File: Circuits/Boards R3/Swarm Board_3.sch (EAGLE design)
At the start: 139 parts, among them CON1 ISP(2X3), CON2 MAIN_CONNECTOR_14SMD, CON4 HEADER_3X1, CON5 HEADER_3X1, CON7 MAIN_CONNECTOR_8, M1 VIBMOTOR, T1 TEFT4300, T10 TEFT4300, T11 NPN2N2222, T12 SI2333DS-T1, T13 NPN2N2222, T14 NPN2N2222, T15 NPN2N2222, T16 NPN2N2222, T17 NPN2N2222, T18 NPN2N2222, T19 IRLML6244TR, T2 TEFT4300, T20 IRLML6244TR, T21 IRLML6244TR, T22 IRLML6244TR, T23 IRLML6244TR, T3 NPN2N2222, T4 TEFT4300, T5 TEFT4300, T6 TEFT4300, T7 TEFT4300, T8 TEFT4300, T9 TEFT4300, U1 ATMEGA324P, U2 MCP73833, U3 ATMEGA1281, U4 MCP9700A, U5 AH182, U6 AH182, U7 QRE1113, U8 QRE1113, U9 QRE1113

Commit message: MORE STUFF
LEDS, TX/RX, WHATEVER
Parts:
- LED11, LED12: value (none) -> RED
- LED14, LED15: value (none) -> GREEN
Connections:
- new net LED5: R56.1
- net LED4: no longer R53.1, R55.1, R56.1
- net MISO: now also R55.1
- net MOSI: now also R53.1
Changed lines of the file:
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@@
 <part name="U9" library="Passive" deviceset="QRE1113" device=""/>
 <part name="R52" library="Passive" deviceset="RES" device="0603" value="100"/>
-<part name="LED11" library="Passive" deviceset="LED" device="0603"/>
+<part name="LED11" library="Passive" deviceset="LED" device="0603" value="RED"/>
 <part name="R53" library="Passive" deviceset="RES" device="0603" value="1k"/>
 <part name="P+3" library="Supply" deviceset="+3V" device=""/>
-<part name="LED12" library="Passive" deviceset="LED" device="0603"/>
+<part name="LED12" library="Passive" deviceset="LED" device="0603" value="RED"/>
 <part name="R54" library="Passive" deviceset="RES" device="0603" value="1k"/>
 <part name="P+8" library="Supply" deviceset="+3V" device=""/>
-<part name="LED14" library="Passive" deviceset="LED" device="0603"/>
+<part name="LED14" library="Passive" deviceset="LED" device="0603" value="GREEN"/>
 <part name="R55" library="Passive" deviceset="RES" device="0603" value="1k"/>
 <part name="P+11" library="Supply" deviceset="+3V" device=""/>
-<part name="LED15" library="Passive" deviceset="LED" device="0603"/>
+<part name="LED15" library="Passive" deviceset="LED" device="0603" value="GREEN"/>
 <part name="R56" library="Passive" deviceset="RES" device="0603" value="1k"/>
 <part name="P+17" library="Supply" deviceset="+3V" device=""/>
@@
 <label x="-53.34" y="38.1" size="1.778" layer="95"/>
 </segment>
+<segment>
+<pinref part="R55" gate="G$1" pin="1"/>
+<wire x1="-86.36" y1="-48.26" x2="-86.36" y2="-50.8" width="0.1524" layer="91"/>
+<label x="-86.36" y="-50.8" size="1.778" layer="91" rot="R270" xref="yes"/>
+</segment>
 </net>
 <net name="TEMPSENSE" class="0">
@@
 <wire x1="-76.2" y1="40.64" x2="-30.48" y2="40.64" width="0.1524" layer="91"/>
 <label x="-53.34" y="40.64" size="1.778" layer="95"/>
+</segment>
+<segment>
+<pinref part="R53" gate="G$1" pin="1"/>
+<wire x1="-106.68" y1="-48.26" x2="-106.68" y2="-50.8" width="0.1524" layer="91"/>
+<label x="-106.68" y="-50.8" size="1.778" layer="91" rot="R270" xref="yes"/>
 </segment>
 </net>
@@
 <net name="LED4" class="0">
 <segment>
-<pinref part="R53" gate="G$1" pin="1"/>
-<wire x1="-106.68" y1="-48.26" x2="-106.68" y2="-50.8" width="0.1524" layer="91"/>
-<label x="-106.68" y="-50.8" size="1.778" layer="91" rot="R270" xref="yes"/>
-</segment>
-<segment>
 <pinref part="R54" gate="G$1" pin="1"/>
 <wire x1="-96.52" y1="-48.26" x2="-96.52" y2="-50.8" width="0.1524" layer="91"/>
 <label x="-96.52" y="-50.8" size="1.778" layer="91" rot="R270" xref="yes"/>
-</segment>
-<segment>
-<pinref part="R55" gate="G$1" pin="1"/>
-<wire x1="-86.36" y1="-48.26" x2="-86.36" y2="-50.8" width="0.1524" layer="91"/>
-<label x="-86.36" y="-50.8" size="1.778" layer="91" rot="R270" xref="yes"/>
-</segment>
-<segment>
-<pinref part="R56" gate="G$1" pin="1"/>
-<wire x1="-76.2" y1="-48.26" x2="-76.2" y2="-50.8" width="0.1524" layer="91"/>
-<label x="-76.2" y="-50.8" size="1.778" layer="91" rot="R270" xref="yes"/>
 </segment>
 </net>
@@
 </segment>
 </net>
+<net name="LED5" class="0">
+<segment>
+<pinref part="R56" gate="G$1" pin="1"/>
+<wire x1="-76.2" y1="-48.26" x2="-76.2" y2="-50.8" width="0.1524" layer="91"/>
+<label x="-76.2" y="-50.8" size="1.778" layer="91" rot="R270" xref="yes"/>
+</segment>
+</net>

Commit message: picked new 3v regulator
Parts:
- added TST1, TST2: TESTPOINT, Mechanical:TESTPOINT
- V1: value MCP1700-3002E -> XC6210B302; device PowerIC:MCP1700-3002E -> PowerIC:XC6210B302
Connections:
- removed net SCL: ANT4.P$1, U3.PD0(SCL/INT0)
- removed net SDA: ANT2.P$1, U3.PD1(SDA/INT1)
- new net CRX: ANT4.P$1, U3.PE0(RXD0/PCINT8/PDI)
- new net CTX: ANT2.P$1, U3.PE1(TXD0/PDO)
- new net DEBUG1: TST1.P$1
- new net DEBUG2: TST2.P$1
- new net VIBE: R58.1
- net +3V: now also C16.1, C9.1, M1.+VM, U$1.VM, V1.VOUT; no longer V1.OUT
- net +VRAW: now also V1.EN, V1.VIN; no longer C16.1, C9.1, M1.+VM, U$1.VM, V1.IN
- net DATAANTENNA: now also U3.PD3(TXD1/INT3); no longer U1.PD1(PCINT25/TXD0)
- net DISTANCELED: no longer R58.1
- net N$8: now also U3.PD2(RXD1/INT2); no longer U1.PD0(PCINT24/RXD0)
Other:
- moved on the sheet: CON5

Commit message: ready to route
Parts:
- removed U9: QRE1113, Passive:QRE1113
- added C17: 10uf, Passive:CAPPTH
- added R25, R59, R6, R60, R61, R62: 10k, Passive:RES0603
- C2: value 10uf -> 1uf; device Passive:CAP0805 -> Passive:CAP0603
- C3, C8: value 1uf -> .1uf
- R34: value 22k -> 10k
- R52: value 100 -> 10k
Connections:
- net IRBUMBER renamed ????
- removed net SIRBUMPER: CON7.5, R34.2, U9.E
- new net LED6: R55.1
- new net LED7: R56.1
- new net N$49: R25.2
- new net N$50: R34.2
- new net N$51: R52.2
- new net N$52: R59.2
- new net N$53: R60.2
- new net N$54: R61.2
- new net N$55: R62.2
- new net N$56: U3.PD0(SCL/INT0)
- new net N$57: U3.PD1(SDA/INT1)
- new net N$58: U3.PE6(T3/INT6)
- new net N$59: U3.PE7(ICP3/CLKO/INT7)
- new net PB0: U3.PB0(!SS!/PCINT0)
- new net PB4: U3.PB4(OC2A/PCINT4)
- new net PB5: U3.PB5(OC1A/PCINT5)
- new net PB6: U3.PB6(OC1B/PCINT6)
- new net PB7: U3.PB7(OC0A/OC1C/PCINT7)
- new net S????: CON7.5
- net +3V: now also C17.1
- net APWM: now also U3.PE3(OC3A/AIN1)
- net BPWM: now also U3.PE4(OC3B/INT4)
- net BUZZER: now also U3.PG5(OC0B)
- net GND: now also C17.2
- net LED4: now also R53.1, U3.PE5(OC3C/INT5); no longer R54.1
- net LED5: now also R54.1; no longer R56.1
- net MISO: no longer R55.1
- net MOSI: no longer R53.1
- net N$2: no longer R52.2
- net N$42: now also R6.2; no longer R52.1, U9.CT
- net RX1: now also R6.1
- net RX2: now also R25.1
- net RX3: now also R34.1
- net RX4: now also R52.1
- net RX5: now also R59.1
- net RX6: now also R60.1
- net RX7: now also R61.1
- net RX8: now also R62.1
- net S+VSENSE: no longer U9.AN, U9.C
- net SGND: no longer R34.1
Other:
- moved on the sheet: C2, R34, R52, U3

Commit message: more routing
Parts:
- removed U1: ATMEGA324P, DigitalIC:ATMEGA324P
- C17: device Passive:CAPPTH -> Passive:CAP0805
- C9: value 1uf -> 10uf; device Passive:CAP0603 -> Passive:CAP0805
- CON2: value MAIN_CONNECTOR_14SMD -> MAIN_CONNECTOR_14; device Mechanical:MAIN_CONNECTOR_14SMD -> Mechanical:MAIN_CONNECTOR_14
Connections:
- removed net IRBUMPER: U1.PA3(ADC3/PCINT3)
- new net N$60: U3.PC0(A8)
- new net N$61: U3.PC1(A9)
- new net N$62: U3.PC2(A10)
- new net N$63: U3.PC3(A11)
- new net N$64: U3.PC4(A12)
- new net N$65: U3.PC5(A13)
- new net N$66: U3.PC6(A14)
- new net N$67: U3.PC7(A15)
- new net N$68: U3.PD4(ICP1)
- new net N$69: U3.PD5(XCK1)
- new net N$70: U3.PD6(T1)
- new net N$71: U3.PD7(T0)
- new net N$72: U3.PF0(ADC0)
- new net N$73: U3.PF1(ADC1)
- new net N$74: U3.PF2(ADC2)
- new net N$75: U3.PF3(ADC3)
- new net N$76: U3.PF4(ADC4/TCK)
- new net N$77: U3.PF5(ADC5/TMS)
- new net N$78: U3.PF6(ADC6/TDO)
- new net N$79: U3.PF7(ADC7/TDI)
- new net N$80: U3.PG0(!WR!)
- new net N$81: U3.PG1(!RD!)
- new net N$82: U3.PG2(ALE)
- new net N$83: U3.PG3(TOSC2)
- new net N$84: U3.PG4(TOSC1)
- new net N$85: U3.PA0(AD0)
- new net N$86: U3.PA1(AD1)
- new net N$87: U3.PA2(AD2)
- new net N$88: U3.PA3(AD3)
- new net N$89: U3.PA4(AD4)
- new net N$90: U3.PA5(AD5)
- new net N$91: U3.PA6(AD6)
- new net N$92: U3.PA7(AD7)
- net AIN1: no longer U1.PD5(PCINT29/OC1A)
- net AIN2: no longer U1.PC0(PCINT16/SCL)
- net APWM: no longer U1.PD7(PCINT31/OC2A)
- net BIN1: no longer U1.PD3(PCINT27/TXD1/INT1)
- net BIN2: no longer U1.PD2(PCINT26/RXD1/INT0)
- net BPWM: no longer U1.PD6(PCINT30/OC2B/ICP)
- net BUZZER: no longer U1.PB4(!SS!/OC0B/PCINT12)
- net CHGDETECT: no longer U1.PB0(XCK0/T0/PCINT8)
- net CHGSTATUS: no longer U1.PB1(T1/CLKO/PCINT9)
- net DISTANCELED: no longer U1.PA6(ADC6/PCINT6)
- net DISTANCERECEIVE: no longer U1.PA7(ADC7/PCINT7)
- net IRENABLE: no longer U1.PA4(ADC4/PCINT4)
- net LED1: no longer U1.PB2(AIN0/INT2/PCINT10)
- net LED2: no longer U1.PB3(AIN1/OC0A/PCINT11)
- net LIGHTSENSE: no longer U1.PA5(ADC5/PCINT5)
- net LINESENSE1: no longer U1.PA1(ADC1/PCINT1)
- net LINESENSE2: no longer U1.PA2(ADC2/PCINT2)
- net RX1: no longer U1.PC2(PCINT18/TCK)
- net RX2: no longer U1.PC3(PCINT19/TMS)
- net RX3: no longer U1.PC4(TDO/PCINT20)
- net RX4: no longer U1.PC5(TDI/PCINT21)
- net RX5: no longer U1.PC6(TOSC1/PCINT22)
- net RX6: no longer U1.PC7(TOSC2/PCINT23)
- net STBY: no longer U1.PD4(PCINT28/XCK1/OC1B)
- net TRANSMITLEDS: no longer U1.PC1(PCINT17/SDA)
- net VBATSENSE: no longer U1.PA0(ADC0/PCINT0)
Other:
- moved on the sheet: C8, C9

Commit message: more routing
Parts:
- added W1, W2, W3: WHISKER, Mechanical:WHISKER
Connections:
- removed net ????: CON2.12
- removed net N$40: R48.1
- removed net N$41: R49.1
- removed net N$42: R6.2
- removed net N$49: R25.2
- removed net N$50: R34.2
- removed net N$51: R52.2
- removed net N$52: R59.2
- removed net N$53: R60.2
- removed net N$54: R61.2
- removed net N$55: R62.2
- removed net N$56: U3.PD0(SCL/INT0)
- removed net N$57: U3.PD1(SDA/INT1)
- removed net N$60: U3.PC0(A8)
- removed net N$61: U3.PC1(A9)
- removed net N$62: U3.PC2(A10)
- removed net N$63: U3.PC3(A11)
- removed net N$64: U3.PC4(A12)
- removed net N$65: U3.PC5(A13)
- removed net N$66: U3.PC6(A14)
- removed net N$67: U3.PC7(A15)
- removed net N$68: U3.PD4(ICP1)
- removed net N$72: U3.PF0(ADC0)
- removed net N$73: U3.PF1(ADC1)
- removed net N$74: U3.PF2(ADC2)
- removed net N$75: U3.PF3(ADC3)
- removed net N$76: U3.PF4(ADC4/TCK)
- removed net N$77: U3.PF5(ADC5/TMS)
- removed net N$78: U3.PF6(ADC6/TDO)
- removed net N$79: U3.PF7(ADC7/TDI)
- removed net N$81: U3.PG1(!RD!)
- removed net N$85: U3.PA0(AD0)
- removed net N$86: U3.PA1(AD1)
- removed net N$87: U3.PA2(AD2)
- removed net N$88: U3.PA3(AD3)
- removed net N$89: U3.PA4(AD4)
- removed net N$90: U3.PA5(AD5)
- removed net N$91: U3.PA6(AD6)
- removed net N$92: U3.PA7(AD7)
- removed net S????: CON7.5
- removed net SLINSENSE2: R33.2, U7.E
- net AIN1: now also U3.PA4(AD4)
- net AIN2: now also U3.PA3(AD3)
- net BIN1: now also U3.PA6(AD6)
- net BIN2: now also U3.PA7(AD7)
- net CHGDETECT: now also U3.PF2(ADC2)
- net CHGSTATUS: now also U3.PF1(ADC1)
- net DISTANCELED: now also U3.PA1(AD1)
- net DISTANCERECEIVE: now also U3.PF5(ADC5/TMS)
- net ENCA: now also U3.PD0(SCL/INT0)
- net ENCB: now also U3.PD1(SDA/INT1)
- net IRENABLE: now also U3.PC7(A15)
- net LED1: now also U3.PC4(A12)
- net LED2: now also U3.PC3(A11)
- net LED3: now also U3.PC2(A10)
- net LED5: now also U3.PG1(!RD!)
- net LED6: now also U3.PC0(A8)
- net LED7: now also U3.PA2(AD2)
- net LEFTBUMPER: now also U3.PC5(A13)
- net LIGHTSENSE: now also U3.PF6(ADC6/TDO)
- net LINESENSE1: now also U3.PF3(ADC3)
- net LINESENSE2: now also U3.PF4(ADC4/TCK)
- net MISO: now also R61.2
- net MOSI: now also R6.2
- net PB0: now also R34.2
- net PB4: now also R60.2
- net PB5: now also R59.2
- net PB6: now also R52.2
- net PB7: now also R62.2
- net RIGHTBUMPER: now also U3.PC6(A14)
- net S+VSENSE: now also W3.P$1; no longer R48.2, R49.2
- net SCK: now also R25.2
- net SEN: now also U3.PE2(XCK0/AIN0)
- net SGND: now also R48.1, R49.1
- net SLEFTBUMPER: now also R49.2, W1.P$1
- net SLINESENSE2: now also R33.2, U7.E
- net SRIGHTBUMPER: now also R48.2, W2.P$1
- net STBY: now also U3.PA5(AD5)
- net TEMPSENSE: now also U3.PF7(ADC7/TDI)
- net TRANSMITLEDS: now also U3.PD4(ICP1)
- net VBATSENSE: now also U3.PF0(ADC0)
- net VIBE: now also U3.PC1(A9)
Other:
- moved on the sheet: R48, R49

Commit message: schematic at 100%
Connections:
- removed net N$58: U3.PE6(T3/INT6)
- removed net N$59: U3.PE7(ICP3/CLKO/INT7)
- removed net N$69: U3.PD5(XCK1)
- removed net N$70: U3.PD6(T1)
- removed net N$71: U3.PD7(T0)
- removed net N$80: U3.PG0(!WR!)
- removed net N$82: U3.PG2(ALE)
- removed net N$83: U3.PG3(TOSC2)
- removed net N$84: U3.PG4(TOSC1)
- net DEBUG1: now also U3.PG2(ALE)
- net DEBUG2: now also U3.PG0(!WR!)
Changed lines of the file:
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@@
 <pinref part="TST1" gate="G$1" pin="P$1"/>
+</segment>
+<segment>
+<pinref part="U3" gate="G$1" pin="PG2(ALE)"/>
+<wire x1="38.1" y1="-33.02" x2="40.64" y2="-33.02" width="0.1524" layer="91"/>
+<label x="40.64" y="-33.02" size="1.778" layer="91" xref="yes"/>
 </segment>
 </net>
@@
 <label x="-50.8" y="-50.8" size="1.778" layer="91" rot="R270" xref="yes"/>
 <pinref part="TST2" gate="G$1" pin="P$1"/>
+</segment>
+<segment>
+<pinref part="U3" gate="G$1" pin="PG0(!WR!)"/>
+<wire x1="38.1" y1="-27.94" x2="40.64" y2="-27.94" width="0.1524" layer="91"/>
+<label x="40.64" y="-27.94" size="1.778" layer="91" xref="yes"/>
 </segment>
 </net>
@@
 </segment>
 </net>
-<net name="N$58" class="0">
-<segment>
-<pinref part="U3" gate="G$1" pin="PE6(T3/INT6)"/>
-<wire x1="38.1" y1="2.54" x2="40.64" y2="2.54" width="0.1524" layer="91"/>
-<label x="40.64" y="2.54" size="1.778" layer="91" xref="yes"/>
-</segment>
-</net>
-<net name="N$59" class="0">
-<segment>
-<pinref part="U3" gate="G$1" pin="PE7(ICP3/CLKO/INT7)"/>
-<wire x1="38.1" y1="0" x2="40.64" y2="0" width="0.1524" layer="91"/>
-<label x="40.64" y="0" size="1.778" layer="91" xref="yes"/>
-</segment>
-</net>
-<net name="N$69" class="0">
-<segment>
-<pinref part="U3" gate="G$1" pin="PD5(XCK1)"/>
-<wire x1="38.1" y1="27.94" x2="40.64" y2="27.94" width="0.1524" layer="91"/>
-</segment>
-</net>
-<net name="N$70" class="0">
-<segment>
-<pinref part="U3" gate="G$1" pin="PD6(T1)"/>
-<wire x1="38.1" y1="25.4" x2="40.64" y2="25.4" width="0.1524" layer="91"/>
-</segment>
-</net>
-<net name="N$71" class="0">
-<segment>
-<pinref part="U3" gate="G$1" pin="PD7(T0)"/>
-<wire x1="38.1" y1="22.86" x2="40.64" y2="22.86" width="0.1524" layer="91"/>
-</segment>
-</net>
-<net name="N$80" class="0">
-<segment>
-<pinref part="U3" gate="G$1" pin="PG0(!WR!)"/>
-<wire x1="38.1" y1="-27.94" x2="40.64" y2="-27.94" width="0.1524" layer="91"/>
-</segment>
-</net>
-<net name="N$82" class="0">
-<segment>
-<pinref part="U3" gate="G$1" pin="PG2(ALE)"/>
-<wire x1="38.1" y1="-33.02" x2="40.64" y2="-33.02" width="0.1524" layer="91"/>
-</segment>
-</net>
-<net name="N$83" class="0">
-<segment>
-<pinref part="U3" gate="G$1" pin="PG3(TOSC2)"/>
-<wire x1="38.1" y1="-35.56" x2="40.64" y2="-35.56" width="0.1524" layer="91"/>
-</segment>
-</net>
-<net name="N$84" class="0">
-<segment>
-<pinref part="U3" gate="G$1" pin="PG4(TOSC1)"/>
-<wire x1="38.1" y1="-38.1" x2="40.64" y2="-38.1" width="0.1524" layer="91"/>
-</segment>
-</net>

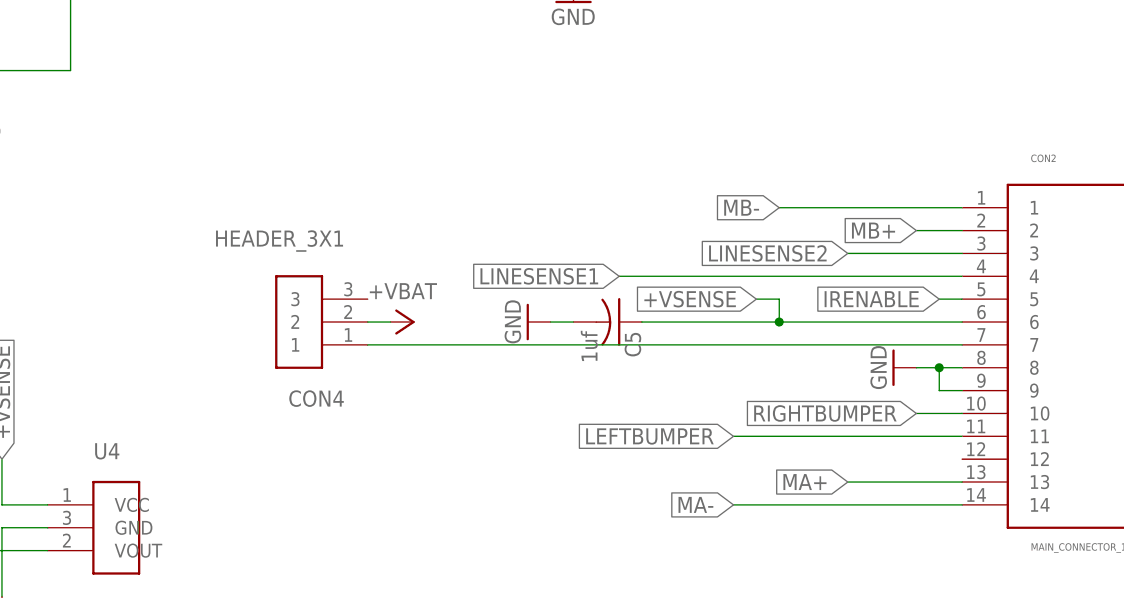
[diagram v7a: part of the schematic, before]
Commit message: adjusted silkscreen and added power switch
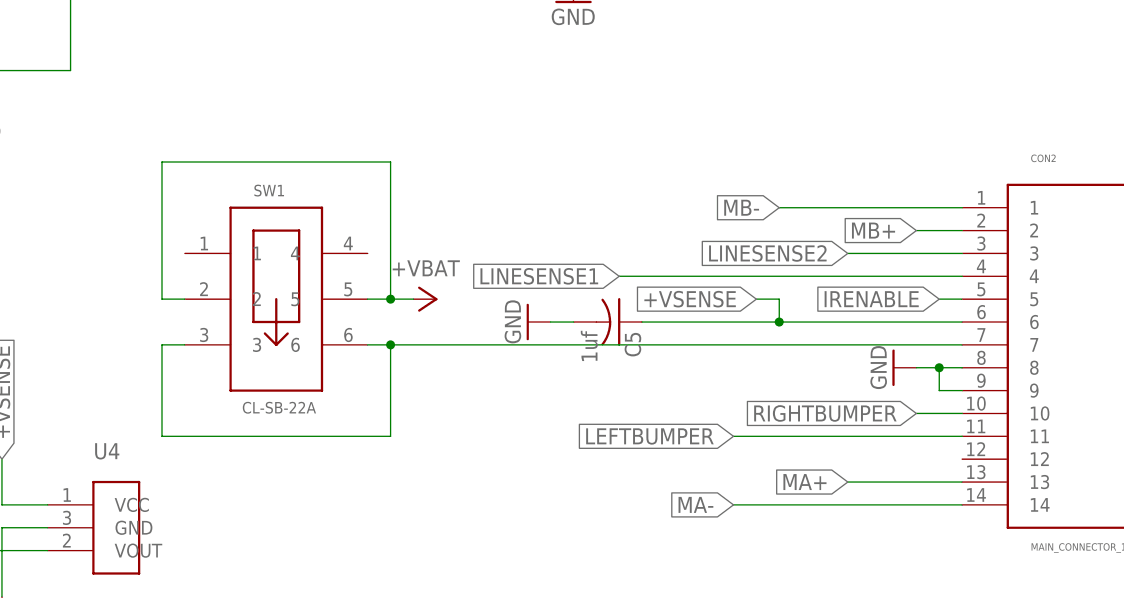
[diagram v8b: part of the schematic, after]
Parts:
- removed CON4: HEADER_3X1, Mechanical:HEADER_3X1
- added SW1: CL-SB-22A, Mechanical:CL-SB-22A
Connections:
- net +VBAT: now also SW1.2, SW1.5; no longer CON4.2
- net N$5: now also SW1.3, SW1.6; no longer CON4.1
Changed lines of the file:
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@@
 <part name="B1" library="Passive" deviceset="PIEZOBUZZER" device="PTH"/>
 <part name="P+4" library="Supply" deviceset="+3V" device=""/>
-<part name="CON4" library="Mechanical" deviceset="HEADER_3X1" device=""/>
 <part name="P+16" library="Supply" deviceset="+VBAT" device=""/>
 <part name="LED10" library="Passive" deviceset="SMD_RGB" device=""/>
@@
 <part name="W2" library="Mechanical" deviceset="WHISKER" device=""/>
 <part name="W3" library="Mechanical" deviceset="WHISKER" device=""/>
+<part name="SW1" library="Mechanical" deviceset="CL-SB-22A" device=""/>
 </parts>
 <sheets>
@@
 <instance part="B1" gate="G$1" x="-119.38" y="35.56"/>
 <instance part="P+4" gate="1" x="-71.12" y="30.48" rot="R270"/>
-<instance part="CON4" gate="G$1" x="193.04" y="-53.34" rot="R180"/>
-<instance part="P+16" gate="G$1" x="200.66" y="-53.34" rot="R270"/>
+<instance part="P+16" gate="G$1" x="203.2" y="-50.8" rot="R270"/>
 <instance part="LED10" gate="G$1" x="-132.08" y="-30.48"/>
 <instance part="P+20" gate="G$1" x="-132.08" y="-22.86"/>
@@
 <instance part="W2" gate="G$1" x="454.66" y="-127" rot="R90"/>
 <instance part="W3" gate="G$1" x="449.58" y="-114.3" rot="R270"/>
+<instance part="SW1" gate="G$1" x="185.42" y="-50.8"/>
 </instances>
 <busses>
@@
 </segment>
 <segment>
-<pinref part="CON4" gate="G$1" pin="2"/>
-<wire x1="198.12" y1="-53.34" x2="200.66" y2="-53.34" width="0.1524" layer="91"/>
+<wire x1="198.12" y1="-50.8" x2="200.66" y2="-50.8" width="0.1524" layer="91"/>
 <pinref part="P+16" gate="G$1" pin="+VBAT"/>
+<pinref part="SW1" gate="G$1" pin="5"/>
+<pinref part="SW1" gate="G$1" pin="2"/>
+<wire x1="200.66" y1="-50.8" x2="203.2" y2="-50.8" width="0.1524" layer="91"/>
+<wire x1="177.8" y1="-50.8" x2="175.26" y2="-50.8" width="0.1524" layer="91"/>
+<wire x1="175.26" y1="-50.8" x2="175.26" y2="-35.56" width="0.1524" layer="91"/>
+<wire x1="175.26" y1="-35.56" x2="200.66" y2="-35.56" width="0.1524" layer="91"/>
+<wire x1="200.66" y1="-35.56" x2="200.66" y2="-50.8" width="0.1524" layer="91"/>
+<junction x="200.66" y="-50.8"/>
 </segment>
 </net>
@@
 <net name="N$5" class="0">
 <segment>
-<pinref part="CON4" gate="G$1" pin="1"/>
 <pinref part="CON2" gate="G$1" pin="7"/>
-<wire x1="198.12" y1="-55.88" x2="264.16" y2="-55.88" width="0.1524" layer="91"/>
-</segment>
-</net>
+<wire x1="198.12" y1="-55.88" x2="200.66" y2="-55.88" width="0.1524" layer="91"/>
+<pinref part="SW1" gate="G$1" pin="6"/>
+<wire x1="200.66" y1="-55.88" x2="264.16" y2="-55.88" width="0.1524" layer="91"/>
+<wire x1="200.66" y1="-55.88" x2="200.66" y2="-66.04" width="0.1524" layer="91"/>
+<wire x1="200.66" y1="-66.04" x2="175.26" y2="-66.04" width="0.1524" layer="91"/>
+<wire x1="175.26" y1="-66.04" x2="175.26" y2="-55.88" width="0.1524" layer="91"/>
+<pinref part="SW1" gate="G$1" pin="3"/>
+<wire x1="175.26" y1="-55.88" x2="177.8" y2="-55.88" width="0.1524" layer="91"/>
+<junction x="200.66" y="-55.88"/>
+</segment>
+</net>
